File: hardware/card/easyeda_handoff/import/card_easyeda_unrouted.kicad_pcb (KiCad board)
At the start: 4 copper layers, 116 x 106 mm, 48 parts, among them J1 HRO-TYPE-C-31-M-12, J2 1S-Pouch-403048, J3 FFC-15-1.0-FH12-class, J4 microSD, Q1 NPN, SW1 TL3315NF160Q-class, SW10A EVP-AKE31A, SW10B EVP-AKE31A, SW2 TL3315NF160Q-class, SW3 TL3315NF160Q-class, SW4 TL3315NF160Q-class, SW5 KMR211NG, SW6 KMR211NG, SW7 KMR211NG, SW8 KMR211NG, SW9 SlideSwitch-SPDT-JS102000-cla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, U1 ESP32-P4NRW32X, U2 BQ24075RGTR, U3 MAX17048G+T10, U4 TPS63070, U5 DRV2605LDGS, U6 TPS22919DCK, U8 PiezoHBridge-DNP, U9 QSPI-NOR-32MB, X1 40MHz-crystal

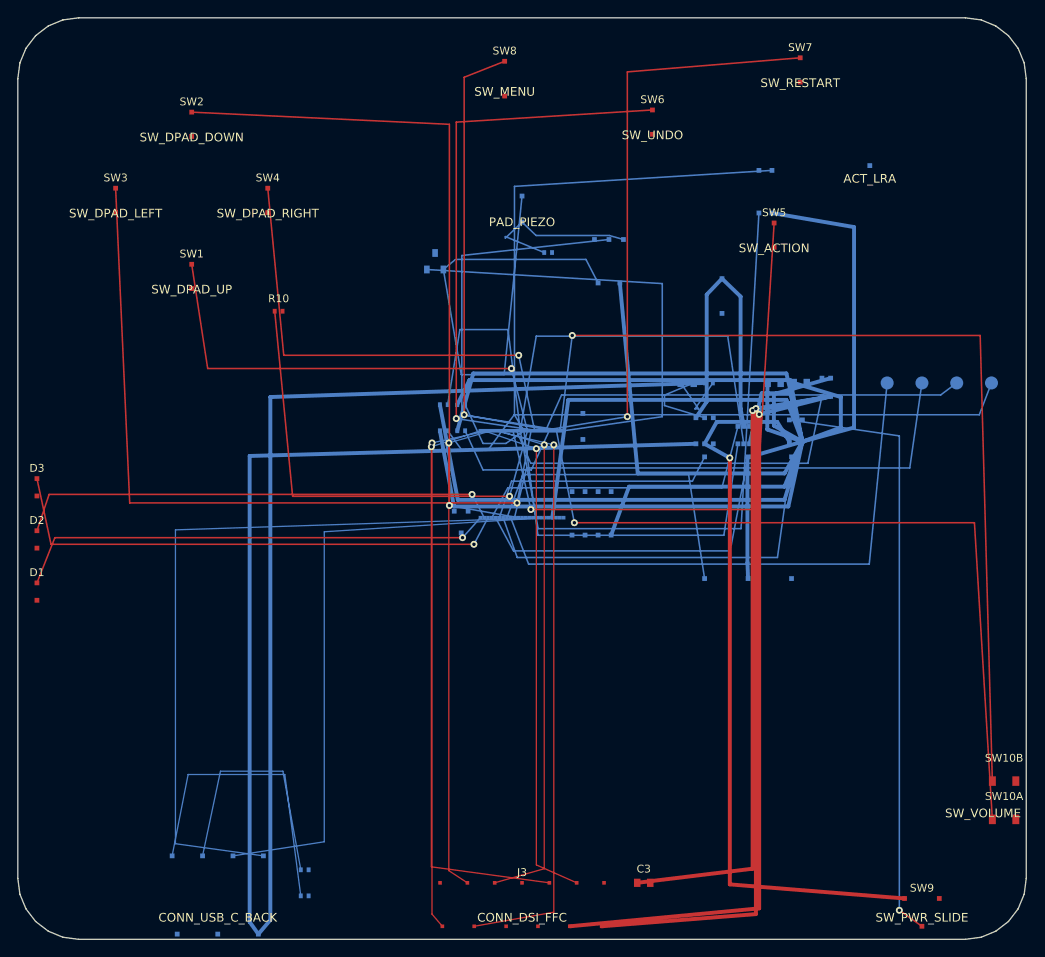
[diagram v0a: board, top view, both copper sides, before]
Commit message: Add handheld card EasyEDA handoff
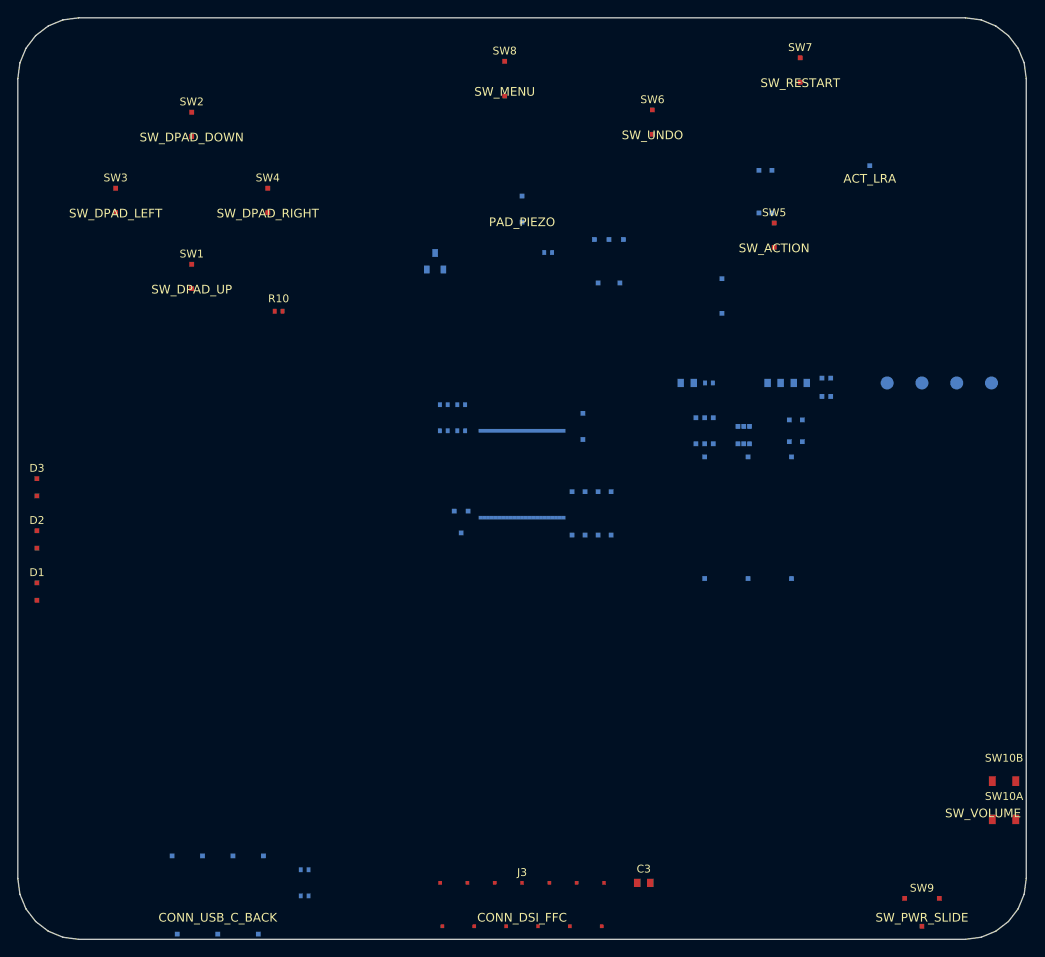
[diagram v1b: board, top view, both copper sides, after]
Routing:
- net +3V3: track 437.2 -> 0.00 mm
- net +3V3_PANEL: track 247.0 -> 0.00 mm, vias 3 -> 0
- net VBUS_IN: track 219.0 -> 0.00 mm
- net I2C_SDA: track 142.8 -> 0.00 mm
- net I2C_SCL: track 112.3 -> 0.00 mm
- net VOL_DOWN: track 109.3 -> 0.00 mm, vias 1 -> 0
- net SW_DPAD_UP: track 108.6 -> 0.00 mm, vias 2 -> 0
- net PIEZO_PWM: track 101.1 -> 0.00 mm
- net VOL_UP: track 91.0 -> 0.00 mm, vias 1 -> 0
- net USB_DP: track 89.3 -> 0.00 mm
- net SW_DPAD_LEFT: track 89.2 -> 0.00 mm, vias 1 -> 0
- net SYS: track 85.0 -> 0.00 mm, vias 1 -> 0
- net SW_DPAD_DOWN: track 81.6 -> 0.00 mm, vias 1 -> 0
- net USB_DM: track 71.7 -> 0.00 mm
- net PWR_EN: track 70.5 -> 0.00 mm, vias 1 -> 0
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
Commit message: puzzlescript hardware case
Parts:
- removed the D2 at (4.20, 62.0)
- removed the SW10A at (115.5, 94.2)
- removed the SW10B at (115.5, 89.8)
- removed the U4 at (91.5, 49.5)
- added C2: 10u, easyeda:C0603, B.Cu at (92.0, 44.0)
- added SW10A: EVP-AKE31A, easyeda:SW-SMD_2P-L3.9-W2.9-P1.90-LS2.8-BR, F.Cu at (115.5, 94.2)
- added SW10B: EVP-AKE31A, easyeda:SW-SMD_2P-L3.9-W2.9-P1.90-LS2.8-BR, F.Cu at (115.5, 89.8)
- added TP1: UART_TX, easyeda:TestPoint_Pad_D1.5mm, B.Cu at (102.0, 44.0)
- B1: footprint PSCard:Preview_B1 -> easyeda:VIBRATING-MOTOR-SMD_WELDING
- C1: footprint PSCard:Fit_C1 -> easyeda:C0603
- C3: footprint PSCard:Fit_C3 -> easyeda:C0603
- D1: footprint PSCard:Preview_D1 -> easyeda:LED0603-RD
- D2: renamed from TP1; value UART_TX -> LED-G; footprint PSCard:Fit_TP1 -> easyeda:LED0603-GN; moved to F.Cu
- D3: footprint PSCard:Preview_D3 -> easyeda:LED0603-FD_BLUE
- D4: renamed from C2; value 10u -> LED-CHG; footprint PSCard:Fit_C2 -> easyeda:LED0603-RD
- J1: footprint PSCard:Fit_J1 -> easyeda:USB-C-SMD_TYPE-C-16PIN-2MD-073
- J2: footprint PSCard:Preview_J2 -> easyeda:CONN-SMD_SM02B-SRSS-TB
- J3: footprint PSCard:Preview_J3 -> easyeda:FPC-SMD_FH12-15S-0.5SH-55
- J4: footprint PSCard:Preview_J4 -> easyeda:TF-015
- JP1: footprint PSCard:Preview_JP1 -> easyeda:TestPoint_Pad_D1.5mm
- L1: value DCDC-inductor -> 2.2uH; footprint PSCard:Preview_L1 -> easyeda:IND-SMD_L4.0-W4.0_HPC4018BM
- Q1: footprint PSCard:Fit_Q1 -> easyeda:SOT-23_L2.9-W1.6-P1.90-LS2.8-BR
- R1: footprint PSCard:Fit_R1 -> easyeda:R0402
- R10: footprint PSCard:Fit_R10 -> easyeda:R0402
- R2: footprint PSCard:Fit_R2 -> easyeda:R0402
- R3: footprint PSCard:Fit_R3 -> easyeda:R0402
- R4: footprint PSCard:Fit_R4 -> easyeda:R0402
- R5: footprint PSCard:Fit_R5 -> easyeda:R0402
- R6: footprint PSCard:Fit_R6 -> easyeda:R0402
- R7: footprint PSCard:Fit_R7 -> easyeda:R0402
- R8: footprint PSCard:Fit_R8 -> easyeda:R0402
- SW1: footprint PSCard:Preview_SW1 -> easyeda:SW-SMD_4P-L4.5-W4.5-P3.00-LS4.5-TL
- SW2: footprint PSCard:Preview_SW2 -> easyeda:SW-SMD_4P-L4.5-W4.5-P3.00-LS4.5-TL
- SW3: footprint PSCard:Preview_SW3 -> easyeda:SW-SMD_4P-L4.5-W4.5-P3.00-LS4.5-TL
- SW4: footprint PSCard:Preview_SW4 -> easyeda:SW-SMD_4P-L4.5-W4.5-P3.00-LS4.5-TL
- SW5: footprint PSCard:Preview_SW5 -> easyeda:SW-SMD_4P-L6.0-W6.0-P4.50-LS6.5-TL
- SW6: footprint PSCard:Preview_SW6 -> easyeda:SW-SMD_4P-L6.0-W6.0-P4.50-LS6.5-TL
- SW7: footprint PSCard:Preview_SW7 -> easyeda:SW-SMD_4P-L6.0-W6.0-P4.50-LS6.5-TL
- SW8: footprint PSCard:Preview_SW8 -> easyeda:SW-SMD_4P-L6.0-W6.0-P4.50-LS6.5-TL
- SW9: footprint PSCard:Preview_SW9 -> easyeda:SW-SMD_6P-L7.0-W3.5-P1.27-LS4.5-TL
- TP2: footprint PSCard:Fit_TP2 -> easyeda:TestPoint_Pad_D1.5mm
- TP3: footprint PSCard:Fit_TP3 -> easyeda:TestPoint_Pad_D1.5mm
- TP4: footprint PSCard:Fit_TP4 -> easyeda:TestPoint_Pad_D1.5mm
- U1: footprint PSCard:Fit_U1 -> easyeda:QFN-104_L10.0-W10.0-P0.35-TL-EP7.5
- U2: footprint PSCard:Fit_U2 -> easyeda:QFN-16_L3.0-W3.0-P0.50-TL-EP1.7
- U3: footprint PSCard:Fit_U3 -> easyeda:TDFN-8_L2.0-W2.0-P0.50-BL-EP1.2
- U4: renamed from D4; value LED-CHG -> TPS63070; footprint PSCard:Fit_D4 -> easyeda:VQFN-HR-15_L3.0-W2.5-P0.50-BL_TPS63070RNMR
- U5: footprint PSCard:Fit_U5 -> easyeda:VSSOP-10_L3.0-W3.0-P0.50-LS4.9-BL
- U6: footprint PSCard:Fit_U6 -> easyeda:SC-70-6_L2.2-W1.3-P0.65-LS2.1-BR
- U8: footprint PSCard:Preview_U8 -> easyeda:W-QFN2020-12_L2.0-W2.0-P0.40-TL-EP0.9
- U9: footprint PSCard:Preview_U9 -> easyeda:WSON-8_L8.0-W6.10-P1.27-BL-EP
- X1: footprint PSCard:Preview_X1 -> easyeda:SMD3225-4P
- moved D2 99.4 mm to (4.20, 62.0)
- moved U4 13.7 mm to (91.5, 49.5)
- moved D4 13.0 mm to (79.0, 44.0)
